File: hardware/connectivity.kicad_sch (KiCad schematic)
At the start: 13 parts, among them J1 USB_C_Receptacle_USB2.0_16P, J2 Raspberry_Pi_2_3, J4 SWD, U2 AMS1117-3.3

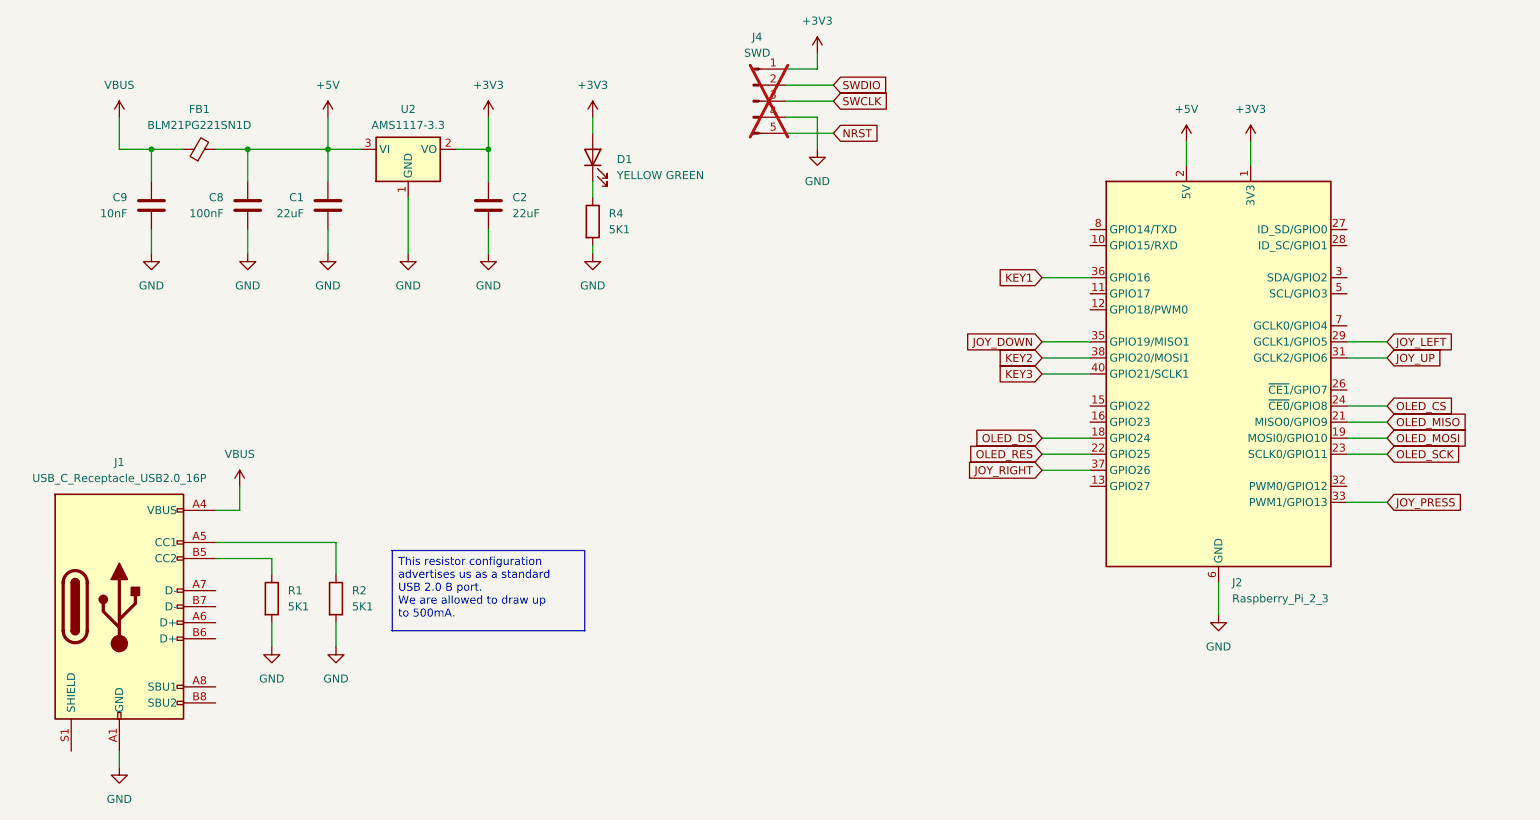
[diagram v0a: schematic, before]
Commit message: Switched to STM32G0B1, improved usage reporting, etc
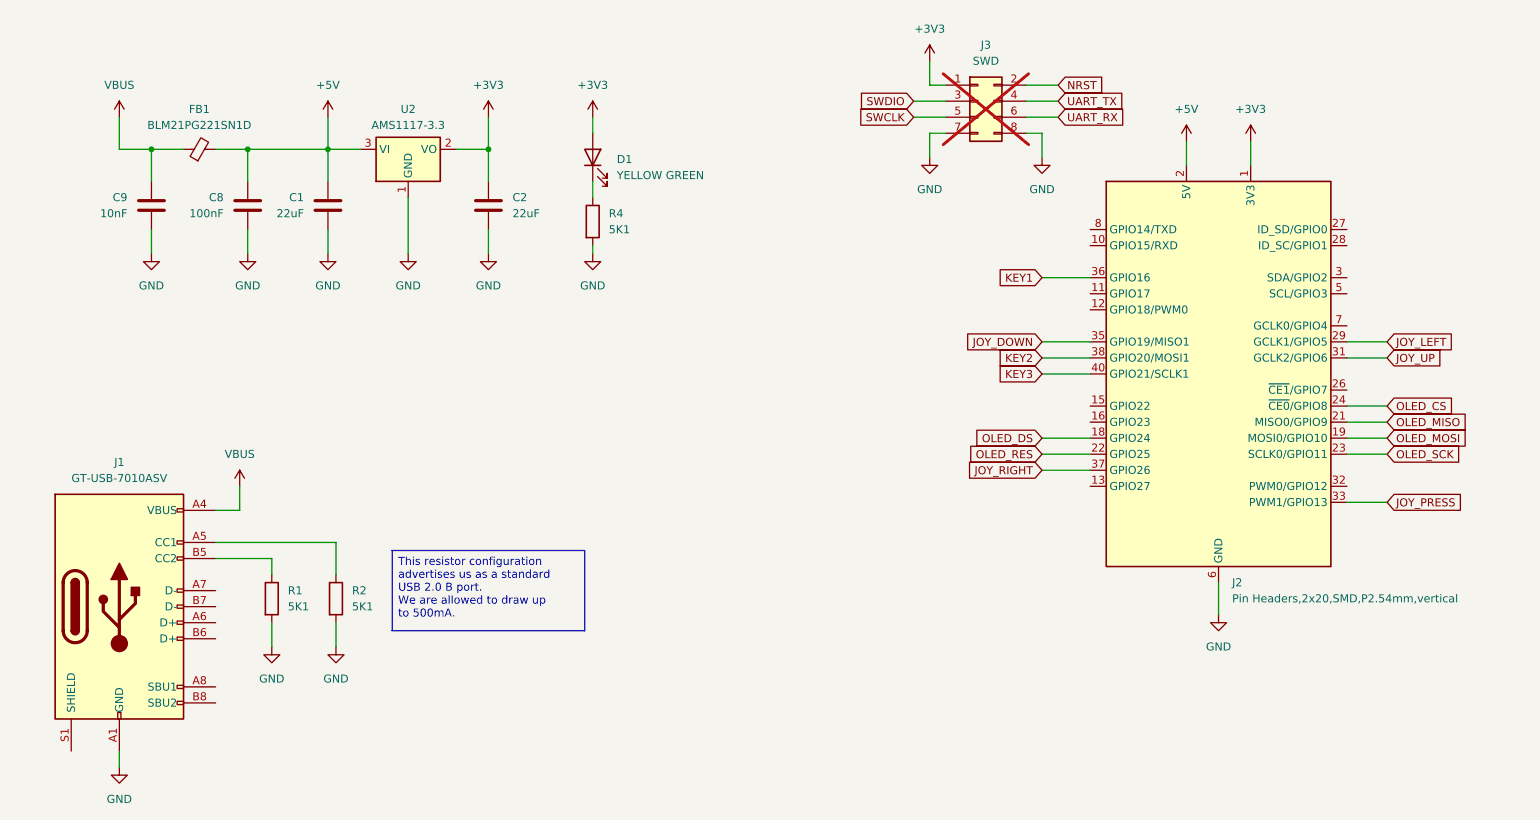
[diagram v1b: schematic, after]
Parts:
- removed J4: SWD, Connector_PinHeader_2.54mm:PinHeader_1x05_P2.54mm_Horizontal, symbol Connector:Conn_01x05_Pin
- added J3: SWD, Connector_PinHeader_2.54mm:PinHeader_2x04_P2.54mm_Horizontal, symbol Connector_Generic:Conn_02x04_Odd_Even
- J1: value USB_C_Receptacle_USB2.0_16P -> GT-USB-7010ASV
- J2: value Raspberry_Pi_2_3 -> Pin Headers,2x20,SMD,P2.54mm,vertical
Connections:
- net +3V3: now also J3.1 (Pin_1)
- net GND: now also J3.7 (Pin_7), J3.8 (Pin_8)
- net NRST: now also J3.2 (Pin_2)
- net SWCLK: now also J3.5 (Pin_5)
- net SWDIO: now also J3.3 (Pin_3)
- new net UART_RX: J3.6 (Pin_6)
- new net UART_TX: J3.4 (Pin_4)

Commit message: Finished board
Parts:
- removed J3: SWD, Connector_PinHeader_2.54mm:PinHeader_2x04_P2.54mm_Horizontal, symbol Connector_Generic:Conn_02x04_Odd_Even
- added J3: SWD, Connector_PinHeader_2.54mm:PinHeader_1x04_P2.54mm_Horizontal, symbol Connector:Conn_01x04_Pin
- J2: footprint Connector_PinHeader_2.54mm:PinHeader_2x20_P2.54mm_Vertical_SMD -> Connector_PinHeader_2.54mm:PinHeader_2x20_P2.54mm_Vertical; now not fitted
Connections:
- net +3V3: now also J3.4 (Pin_4)
- net GND: now also J3.1 (Pin_1)
- net SWCLK: now also J3.2 (Pin_2)
- net SWDIO: now also J3.3 (Pin_3)

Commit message: Reorganized repo
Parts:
- removed J3: SWD, Connector_PinHeader_2.54mm:PinHeader_1x04_P2.54mm_Horizontal, symbol Connector:Conn_01x04_Pin
- added J3: SWD, Connector_PinHeader_2.54mm:PinHeader_1x07_P2.54mm_Horizontal, symbol Connector:Conn_01x07_Pin
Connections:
- net +3V3: now also J3.7 (Pin_7)
- net GND: now also J3.4 (Pin_4)
- net SWCLK: now also J3.5 (Pin_5)
- net SWDIO: now also J3.6 (Pin_6)
- new net NRST: J3.3 (Pin_3)
- new net UART_RX: J3.1 (Pin_1)
- new net UART_TX: J3.2 (Pin_2)
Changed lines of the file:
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@@
 	(wire
 		(pts
-			(xy 160.02 58.42) (xy 160.02 62.23)
+			(xy 160.02 58.42) (xy 160.02 69.85)
 		)
 		(stroke
@@
 	(wire
 		(pts
+			(xy 157.48 60.96) (xy 162.56 60.96)
+		)
+		(stroke
+			(width 0)
+			(type default)
+		)
+	)
+	(wire
+		(pts
 			(xy 46.99 60.96) (xy 52.07 60.96)
 		)
@@
 	(wire
 		(pts
+			(xy 157.48 66.04) (xy 162.56 66.04)
+		)
+		(stroke
+			(width 0)
+			(type default)
+		)
+	)
+	(wire
+		(pts
 			(xy 36.83 60.96) (xy 41.91 60.96)
 		)
@@
 	(wire
 		(pts
+			(xy 157.48 63.5) (xy 162.56 63.5)
+		)
+		(stroke
+			(width 0)
+			(type default)
+		)
+	)
+	(wire
+		(pts
 			(xy 52.07 60.96) (xy 52.07 66.04)
 		)
@@
 		)
 	)
+	(global_label "UART_RX"
+		(shape input)
+		(at 157.48 66.04 180)
+		(fields_autoplaced yes)
+		(effects
+			(font
+				(size 1.27 1.27)
+			)
+			(justify right)
+		)
+		(property "Intersheetrefs" "${INTERSHEET_REFS}"
+			(at 146.391 66.04 0)
+			(effects
+				(font
+					(size 1.27 1.27)
+				)
+				(justify right)
+				(hide yes)
+			)
+		)
+	)
 	(global_label "KEY1"
 		(shape input)
@@
 		)
 	)
+	(global_label "NRST"
+		(shape input)
+		(at 157.48 60.96 180)
+		(fields_autoplaced yes)
+		(effects
+			(font
+				(size 1.27 1.27)
+			)
+			(justify right)
+		)
+		(property "Intersheetrefs" "${INTERSHEET_REFS}"
+			(at 149.7172 60.96 0)
+			(effects
+				(font
+					(size 1.27 1.27)
+				)
+				(justify right)
+				(hide yes)
+			)
+		)
+	)
 	(global_label "JOY_LEFT"
 		(shape input)
@@
 		)
 	)
+	(global_label "UART_TX"
+		(shape input)
+		(at 157.48 63.5 180)
+		(fields_autoplaced yes)
+		(effects
+			(font
+				(size 1.27 1.27)
+			)
+			(justify right)
+		)
+		(property "Intersheetrefs" "${INTERSHEET_REFS}"
+			(at 146.6934 63.5 0)
+			(effects
+				(font
+					(size 1.27 1.27)
+				)
+				(justify right)
+				(hide yes)
+			)
+		)
+	)
 	(global_label "KEY3"
 		(shape input)
@@
 	(symbol
 		(lib_id "power:GND")
-		(at 160.02 62.23 0)
+		(at 160.02 69.85 0)
 		(unit 1)
 		(exclude_from_sim no)
@@
 		(fields_autoplaced yes)
 		(property "Reference" "#PWR029"
-			(at 160.02 68.58 0)
+			(at 160.02 76.2 0)
 			(effects
 				(font
@@
 		)
 		(property "Value" "GND"
-			(at 160.02 67.31 0)
+			(at 160.02 74.93 0)
 			(effects
 				(font
@@
 		)
 		(property "Footprint" ""
-			(at 160.02 62.23 0)
+			(at 160.02 69.85 0)
 			(effects
 				(font
@@
 		)
 		(property "Datasheet" ""
-			(at 160.02 62.23 0)
+			(at 160.02 69.85 0)
 			(effects
 				(font
@@
 		)
 		(property "Description" "Power symbol creates a global label with name \"GND\" , ground"
-			(at 160.02 62.23 0)
+			(at 160.02 69.85 0)
 			(effects
 				(font
@@
 	)
 	(symbol
-		(lib_id "Connector:Conn_01x04_Pin")
-		(at 167.64 55.88 180)
-		(unit 1)
-		(exclude_from_sim no)
-		(in_bom yes)
-		(on_board yes)
-		(dnp yes)
-		(property "Reference" "J3"
-			(at 168.91 53.3399 0)
-			(effects
-				(font
-					(size 1.27 1.27)
-				)
-				(justify right)
-			)
-		)
-		(property "Value" "SWD"
-			(at 168.91 55.8799 0)
-			(effects
-				(font
-					(size 1.27 1.27)
-				)
-				(justify right)
-			)
-		)
-		(property "Footprint" "Connector_PinHeader_2.54mm:PinHeader_1x04_P2.54mm_Horizontal"
-			(at 166.624 39.116 0)
-			(effects
-				(font
-					(size 1.27 1.27)
-				)
-				(hide yes)
-			)
-		)
-		(property "Datasheet" "~"
-			(at 167.64 55.88 0)
-			(effects
-				(font
-					(size 1.27 1.27)
-				)
-				(hide yes)
-			)
-		)
-		(property "Description" "Generic connector, single row, 01x04, script generated"
-			(at 167.64 55.88 0)
-			(effects
-				(font
-					(size 1.27 1.27)
-				)
-				(hide yes)
-			)
-		)
-		(pin "3"
-		)
-		(pin "2"
-		)
-		(pin "1"
-		)
-		(pin "4"
-		)
-		(instances
-			(project ""
-				(path "/301ddcee-4740-4eda-b689-6f23930b1798/318b2e69-26c4-459c-82f8-99b530565fe2"
-					(reference "J3")
-					(unit 1)
-				)
-			)
-		)
-	)
-	(symbol
 		(lib_id "power:+3V3")
 		(at 160.02 46.99 0)
@@
 					(unit 1)
 				)
+			)
+		)
+	)
+	(symbol
+		(lib_id "Connector:Conn_01x07_Pin")
+		(at 167.64 58.42 180)
+		(unit 1)
+		(exclude_from_sim no)
+		(in_bom yes)
+		(on_board yes)
+		(dnp no)
+		(fields_autoplaced yes)
+		(property "Reference" "J3"
+			(at 168.91 57.1499 0)
+			(effects
+				(font
+					(size 1.27 1.27)
+				)
+				(justify right)
+			)
+		)
+		(property "Value" "SWD"
+			(at 168.91 59.6899 0)
+			(effects
+				(font
+					(size 1.27 1.27)
+				)
+				(justify right)
+			)
+		)
+		(property "Footprint" "Connector_PinHeader_2.54mm:PinHeader_1x07_P2.54mm_Horizontal"
+			(at 167.64 58.42 0)
+			(effects
+				(font
+					(size 1.27 1.27)
+				)
+				(hide yes)
+			)
+		)
+		(property "Datasheet" "~"
+			(at 167.64 58.42 0)
+			(effects
+				(font
+					(size 1.27 1.27)
+				)
+				(hide yes)
+			)
+		)
+		(property "Description" "Generic connector, single row, 01x07, script generated"
+			(at 167.64 58.42 0)
+			(effects
+				(font
+					(size 1.27 1.27)
+				)
+				(hide yes)
+			)
+		)
+		(property "LCSC Part #" ""
+			(at 167.64 58.42 0)
+			(effects
+				(font
+					(size 1.27 1.27)
+				)
+				(hide yes)
+			)
+		)
+		(pin "1"
+		)
+		(pin "2"
+		)
+		(pin "3"
+		)
+		(pin "4"
+		)
+		(pin "5"
+		)
+		(pin "6"
+		)
+		(pin "7"
+		)
+		(instances
+			(project ""
+				(path "/301ddcee-4740-4eda-b689-6f23930b1798/318b2e69-26c4-459c-82f8-99b530565fe2"
+					(reference "J3")
+					(unit 1)
+				)
